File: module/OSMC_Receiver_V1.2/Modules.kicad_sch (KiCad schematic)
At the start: 44 parts, among them U2 LTC4317, U5 LTC4317, U6 LTC4317, U7 LTC4317

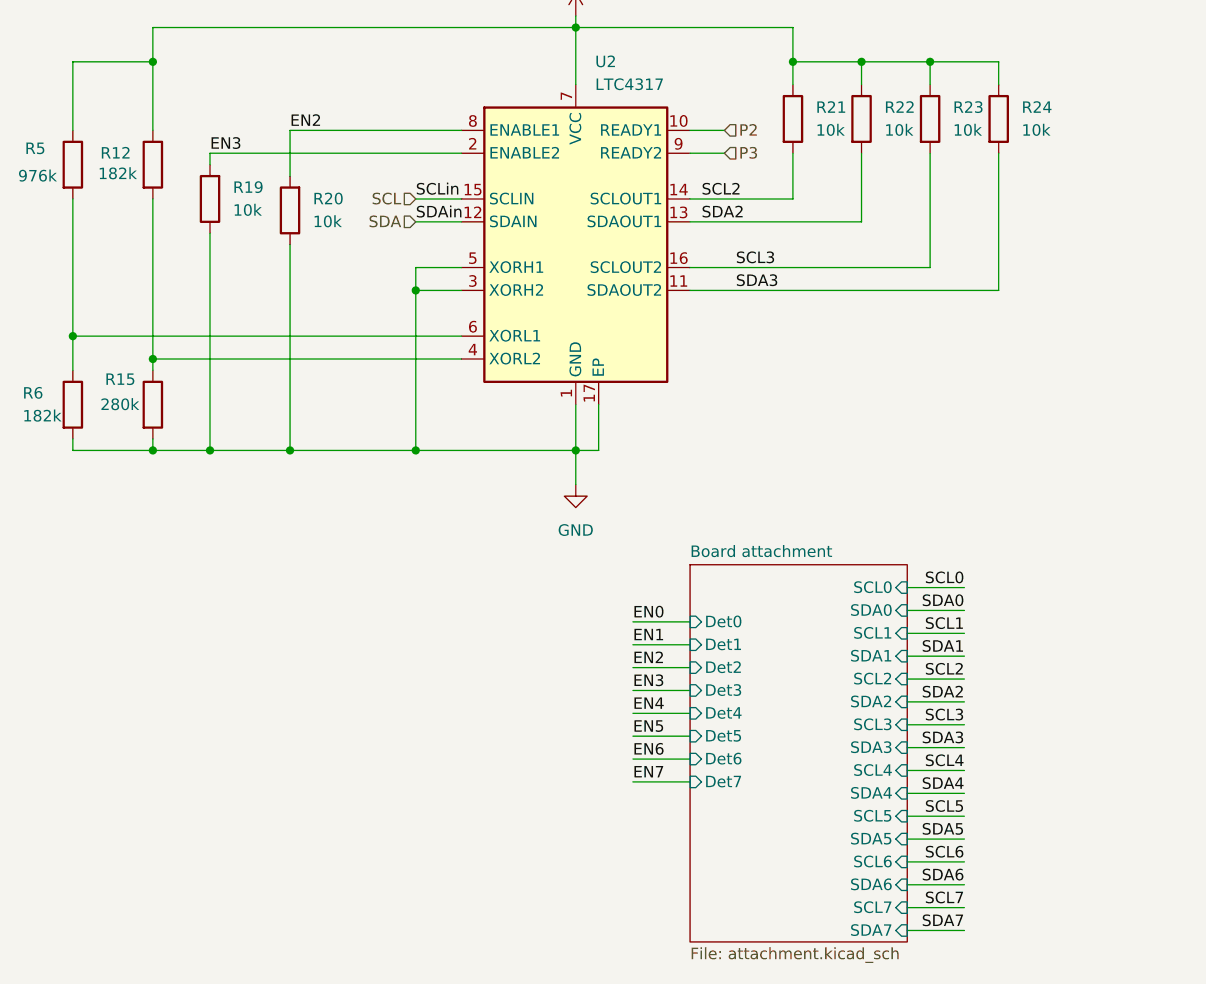
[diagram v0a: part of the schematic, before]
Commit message: update to pcb, fixed i2c lines for bus 0 and 1
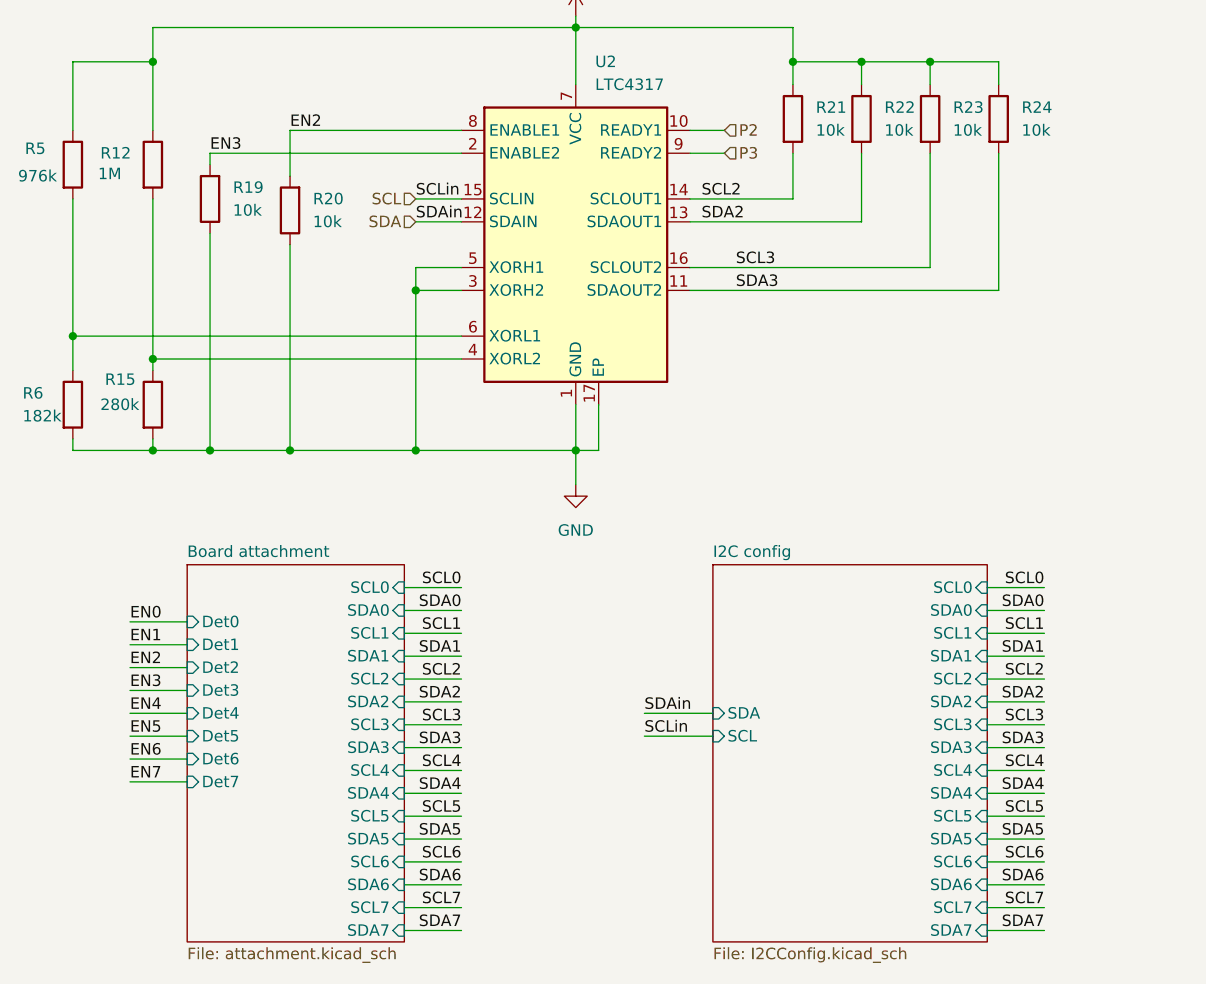
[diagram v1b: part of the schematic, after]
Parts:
- R12: value 182k -> 1M
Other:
- added sheet I2C config (I2CConfig.kicad_sch)

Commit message: board update
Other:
- sheet Board attachment ports: added Opt0, Opt1, Opt2, Opt3, Opt4, Opt5, Opt6, Opt7; removed none
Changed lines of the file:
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@@
 	(wire
 		(pts
-			(xy 29.21 173.99) (xy 35.56 173.99)
+			(xy 29.21 168.91) (xy 35.56 168.91)
 		)
 		(stroke
@@
 	(wire
 		(pts
-			(xy 29.21 171.45) (xy 35.56 171.45)
+			(xy 29.21 166.37) (xy 35.56 166.37)
 		)
 		(stroke
@@
 	(wire
 		(pts
-			(xy 29.21 161.29) (xy 35.56 161.29)
+			(xy 29.21 156.21) (xy 35.56 156.21)
 		)
 		(stroke
@@
 	(wire
 		(pts
-			(xy 29.21 168.91) (xy 35.56 168.91)
+			(xy 29.21 163.83) (xy 35.56 163.83)
 		)
 		(stroke
@@
 	(wire
 		(pts
-			(xy 29.21 166.37) (xy 35.56 166.37)
+			(xy 29.21 161.29) (xy 35.56 161.29)
 		)
 		(stroke
@@
 	(wire
 		(pts
-			(xy 29.21 158.75) (xy 35.56 158.75)
+			(xy 29.21 153.67) (xy 35.56 153.67)
 		)
 		(stroke
@@
 	(wire
 		(pts
-			(xy 29.21 163.83) (xy 35.56 163.83)
+			(xy 29.21 158.75) (xy 35.56 158.75)
 		)
 		(stroke
@@
 	(wire
 		(pts
-			(xy 29.21 176.53) (xy 35.56 176.53)
+			(xy 29.21 171.45) (xy 35.56 171.45)
 		)
 		(stroke
@@
 	)
 	(label "EN2"
-		(at 29.21 163.83 0)
+		(at 29.21 158.75 0)
 		(effects
 			(font
@@
 	)
 	(label "EN4"
-		(at 29.21 168.91 0)
+		(at 29.21 163.83 0)
 		(effects
 			(font
@@
 	)
 	(label "EN3"
-		(at 29.21 166.37 0)
+		(at 29.21 161.29 0)
 		(effects
 			(font
@@
 	)
 	(label "EN5"
-		(at 29.21 171.45 0)
+		(at 29.21 166.37 0)
 		(effects
 			(font
@@
 	)
 	(label "EN6"
-		(at 29.21 173.99 0)
+		(at 29.21 168.91 0)
 		(effects
 			(font
@@
 	)
 	(label "EN7"
-		(at 29.21 176.53 0)
+		(at 29.21 171.45 0)
 		(effects
 			(font
@@
 	)
 	(label "EN1"
-		(at 29.21 161.29 0)
+		(at 29.21 156.21 0)
 		(effects
 			(font
@@
 	)
 	(label "EN0"
-		(at 29.21 158.75 0)
+		(at 29.21 153.67 0)
 		(effects
 			(font
@@
 		)
 		(pin "Det1" input
-			(at 35.56 161.29 180)
+			(at 35.56 156.21 180)
 			(effects
 				(font
@@
 		)
 		(pin "Det2" input
-			(at 35.56 163.83 180)
+			(at 35.56 158.75 180)
 			(effects
 				(font
@@
 		)
 		(pin "Det6" input
-			(at 35.56 173.99 180)
+			(at 35.56 168.91 180)
 			(effects
 				(font
@@
 		)
 		(pin "Det4" input
-			(at 35.56 168.91 180)
+			(at 35.56 163.83 180)
 			(effects
 				(font
@@
 		)
 		(pin "Det5" input
-			(at 35.56 171.45 180)
+			(at 35.56 166.37 180)
 			(effects
 				(font
@@
 		)
 		(pin "Det7" input
-			(at 35.56 176.53 180)
+			(at 35.56 171.45 180)
 			(effects
 				(font
@@
 		)
 		(pin "Det3" input
-			(at 35.56 166.37 180)
+			(at 35.56 161.29 180)
 			(effects
 				(font
@@
 		)
 		(pin "Det0" input
-			(at 35.56 158.75 180)
+			(at 35.56 153.67 180)
 			(effects
 				(font
@@
 			)
 		)
+		(pin "Opt0" input
+			(at 35.56 173.99 180)
+			(effects
+				(font
+					(size 1.27 1.27)
+				)
+				(justify left)
+			)
+		)
+		(pin "Opt1" input
+			(at 35.56 176.53 180)
+			(effects
+				(font
+					(size 1.27 1.27)
+				)
+				(justify left)
+			)
+		)
+		(pin "Opt6" input
+			(at 35.56 189.23 180)
+			(effects
+				(font
+					(size 1.27 1.27)
+				)
+				(justify left)
+			)
+		)
+		(pin "Opt5" input
+			(at 35.56 186.69 180)
+			(effects
+				(font
+					(size 1.27 1.27)
+				)
+				(justify left)
+			)
+		)
+		(pin "Opt3" input
+			(at 35.56 181.61 180)
+			(effects
+				(font
+					(size 1.27 1.27)
+				)
+				(justify left)
+			)
+		)
+		(pin "Opt7" input
+			(at 35.56 191.77 180)
+			(effects
+				(font
+					(size 1.27 1.27)
+				)
+				(justify left)
+			)
+		)
+		(pin "Opt2" input
+			(at 35.56 179.07 180)
+			(effects
+				(font
+					(size 1.27 1.27)
+				)
+				(justify left)
+			)
+		)
+		(pin "Opt4" input
+			(at 35.56 184.15 180)
+			(effects
+				(font
+					(size 1.27 1.27)
+				)
+				(justify left)
+			)
+		)
